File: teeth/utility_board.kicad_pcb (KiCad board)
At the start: 2 copper layers, 100 x 100 mm, 1 part

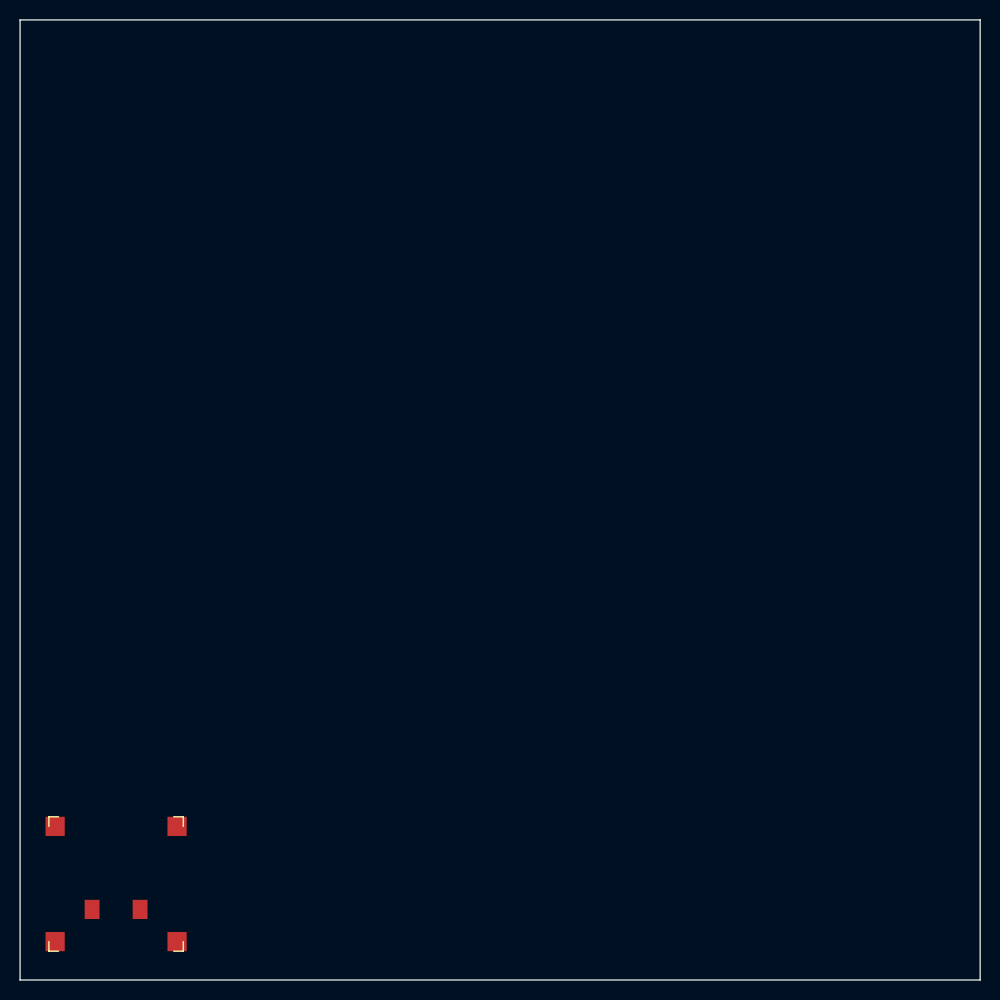
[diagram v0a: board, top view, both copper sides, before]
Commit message: Add xiao cutout footprint to utility board.
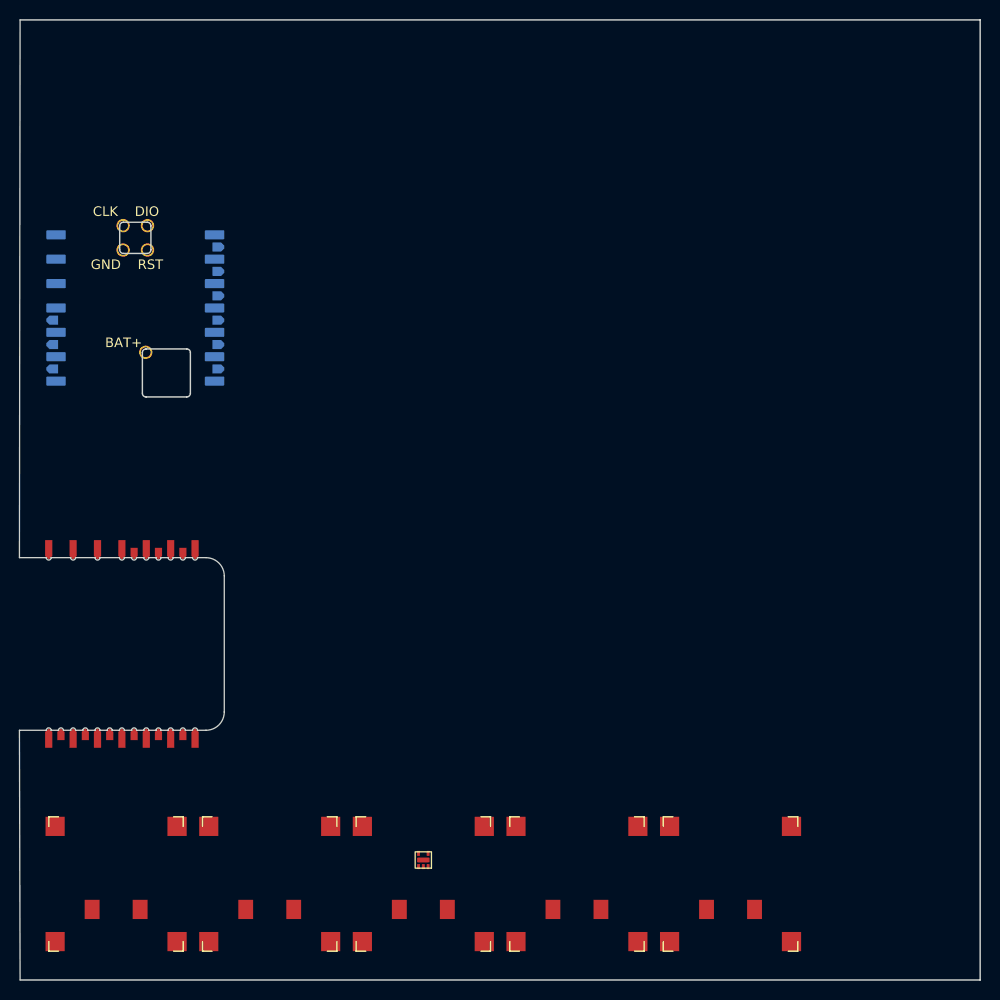
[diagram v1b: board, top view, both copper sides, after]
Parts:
- added D1: , D_MMBD4148PLM, F.Cu at (142.0, 187.5)
- added J1: , xiao_plus_cutout, F.Cu at (110.6, 165.0)
- added S2: , PG1316S, F.Cu at (126.0, 190.0)
- added S3: , PG1316S, F.Cu at (142.0, 190.0)
- added S4: , PG1316S, F.Cu at (158.0, 190.0)
- added S5: , PG1316S, F.Cu at (174.0, 190.0)
- added XX1: , xiao_plus_smd_prod, B.Cu at (112.0, 130.0)
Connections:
- S1 pad 1: firstcol_firstrow -> pinky_home
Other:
- board size 100 x 100 mm -> 100.1 x 100 mm
- net class Default removed

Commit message: More work on utility board, complex xiao slot complete. Fixed email address.
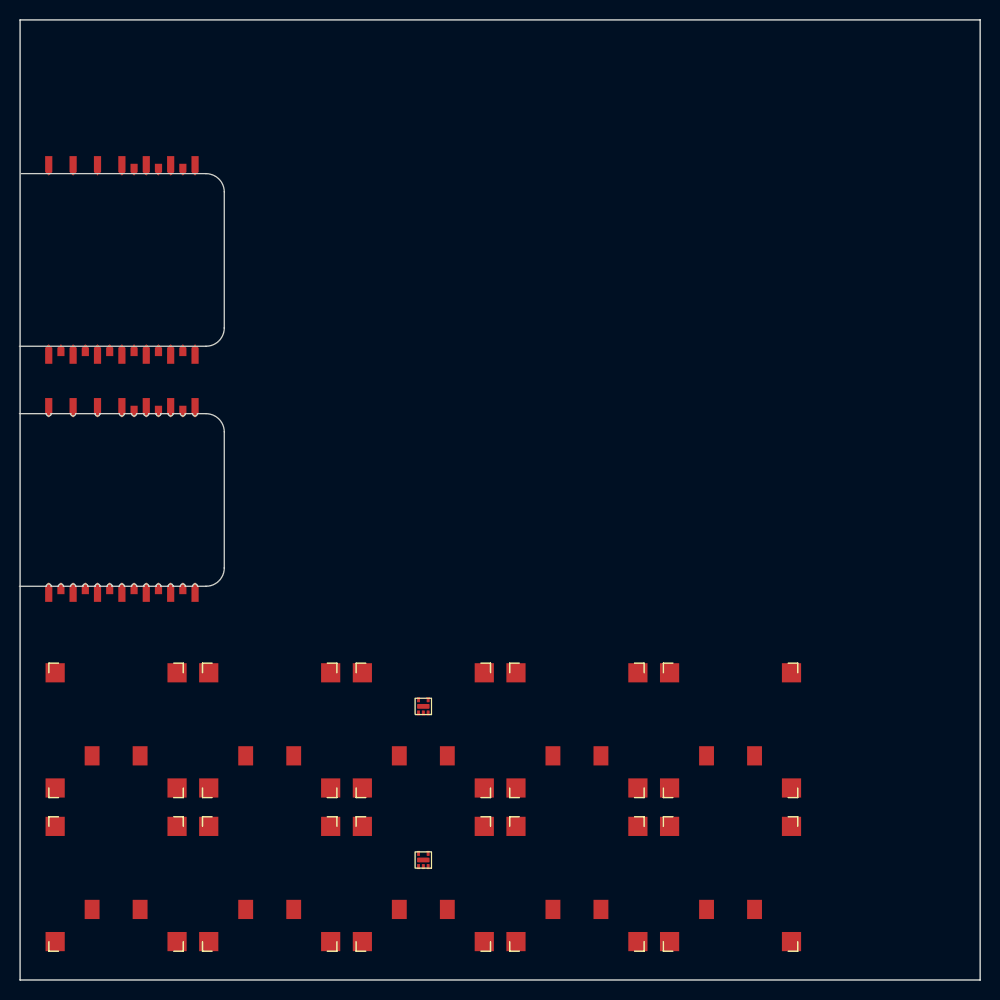
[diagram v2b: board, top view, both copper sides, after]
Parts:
- removed XX1: , xiao_plus_smd_prod
- added D2: , D_MMBD4148PLM, F.Cu at (142.0, 171.5)
- added J2: , xiao_plus_cutout, F.Cu at (110.6, 125.0)
- added S10: , PG1316S, F.Cu at (174.0, 174.0)
- added S6: , PG1316S, F.Cu at (142.0, 174.0)
- added S7: , PG1316S, F.Cu at (158.0, 190.0)
- added S8: , PG1316S, F.Cu at (158.0, 174.0)
- added S9: , PG1316S, F.Cu at (174.0, 190.0)
- moved S4 35.8 mm to (126.0, 174.0)
- moved S5 32.0 mm to (142.0, 190.0)
- moved S2 22.6 mm to (110.0, 174.0)
- moved S3 16.0 mm to (126.0, 190.0)
- moved J1 15.0 mm to (110.6, 150.0)
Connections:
- D1 pad 6: D8 -> P0.03
- S1 pad 2: D5 -> P0.02
- S2 pad 1: ring_home -> pinky_top
- S2 pad 2: D4 -> P0.02
- S3 pad 1: middle_home -> ring_home
- S3 pad 2: D3 -> P0.15
- S4 pad 1: index_home -> ring_top
- S4 pad 2: D2 -> P0.15
- S5 pad 1: inner_home -> middle_home
- S5 pad 2: D1 -> P1.13
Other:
- board size 100.1 x 100 mm -> 100 x 100 mm
- net class Default added: clearance 0.2, trace_width 0.25, via_dia 0.8, via_drill 0.4
